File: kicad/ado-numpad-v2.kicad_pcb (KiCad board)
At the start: 2 copper layers, 99.5 x 96.8 mm, 39 parts, among them J1 Conn_01x04, J2 AudioJack4, SW1 SW_Push, SW10 SW_Push, SW11 SW_Push, SW12 SW_Push, SW13 SW_Push, SW14 SW_Push, SW15 SW_Push, SW16 SW_Push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

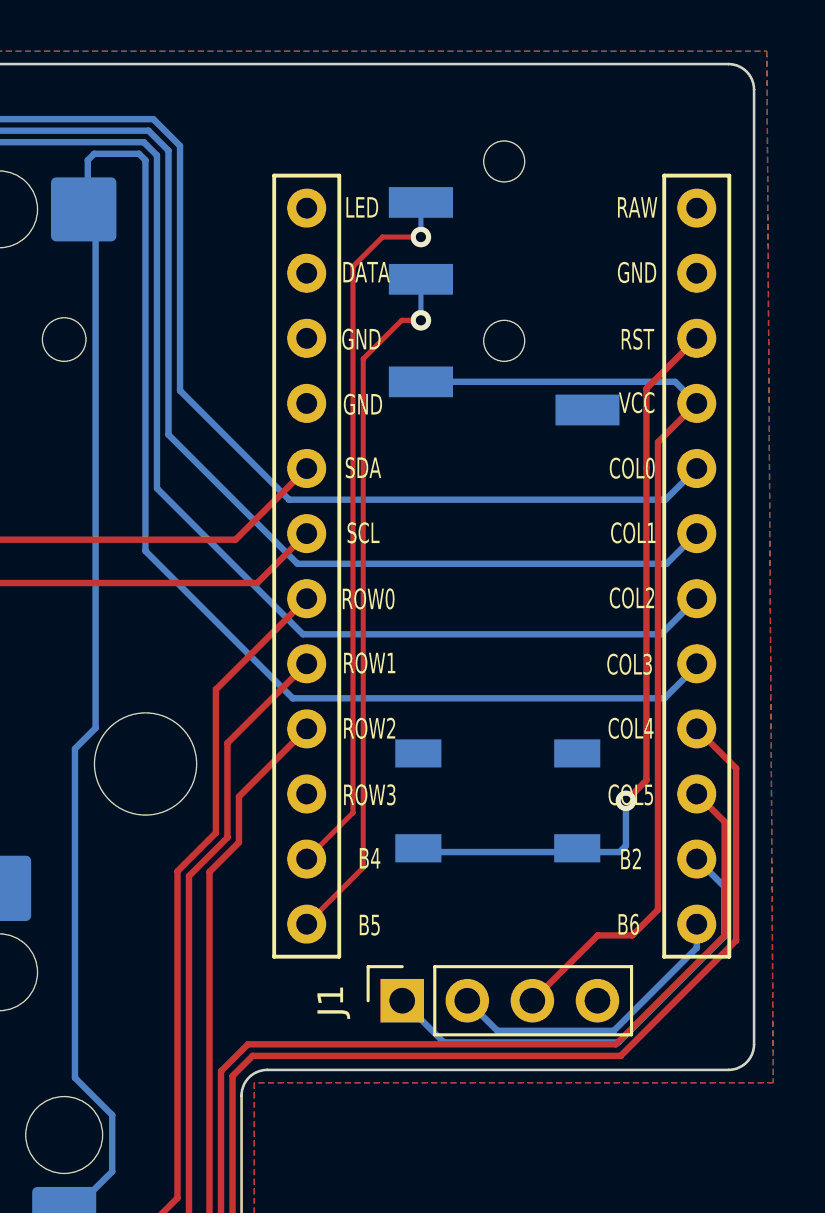
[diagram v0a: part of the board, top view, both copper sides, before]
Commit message: Update to use 2 1x12_P2.54mm Pin Sockets
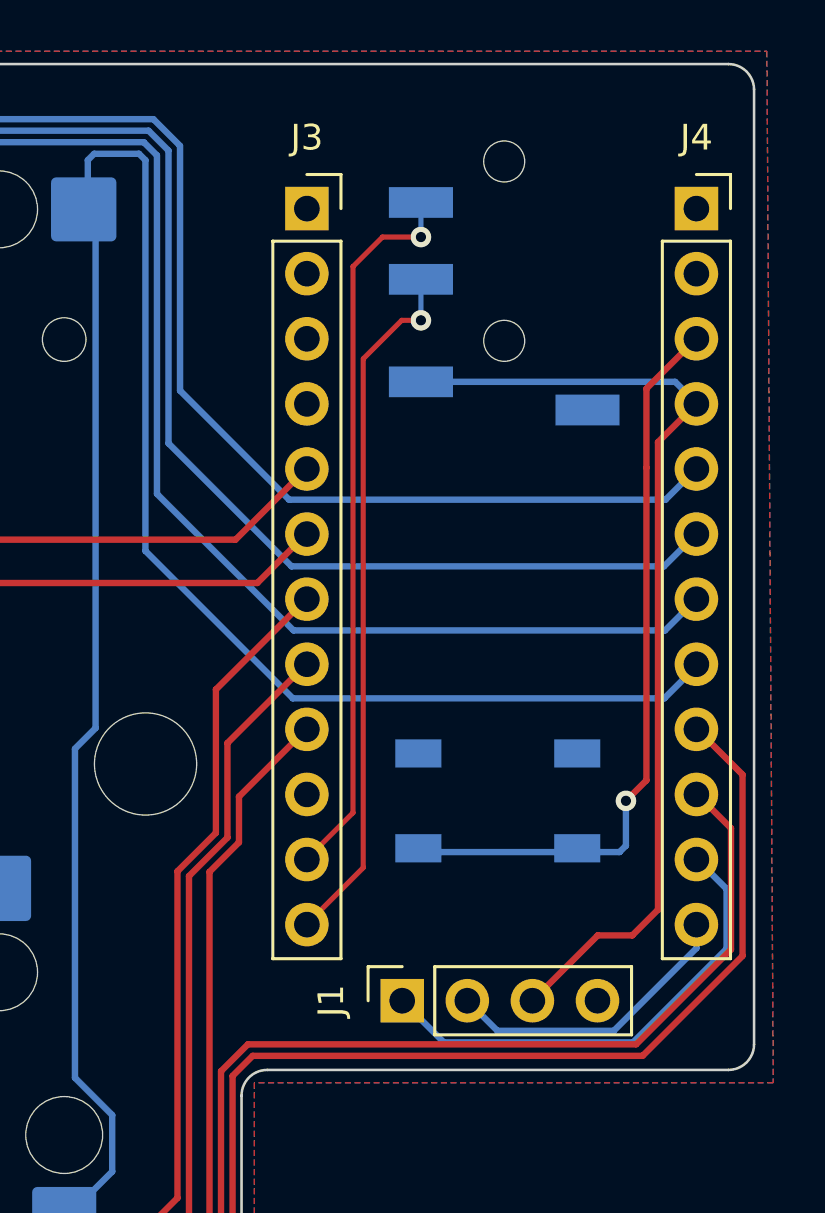
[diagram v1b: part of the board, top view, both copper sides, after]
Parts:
- removed U1: ProMicro, kbd:ProMicro_v2_1side
- added J3: Conn_01x12, Connector_PinSocket_2.54mm:PinSocket_1x12_P2.54mm_Vertical, F.Cu at (172.8, 57.1)
- added J4: Conn_01x12, Connector_PinSocket_2.54mm:PinSocket_1x12_P2.54mm_Vertical, F.Cu at (188.0, 57.1)
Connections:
- SW19 pad 2: RESET -> Net-(J4-Pin_3)
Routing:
- net RESET: track 29.0 -> 0.00 mm, vias 1 -> 0
- net Net-(J4-Pin_3): track 0.00 -> 29.0 mm, vias 0 -> 1
- net Enc_B: track 262.9 -> 263.6 mm
- net Enc_A: track 250.9 -> 251.6 mm

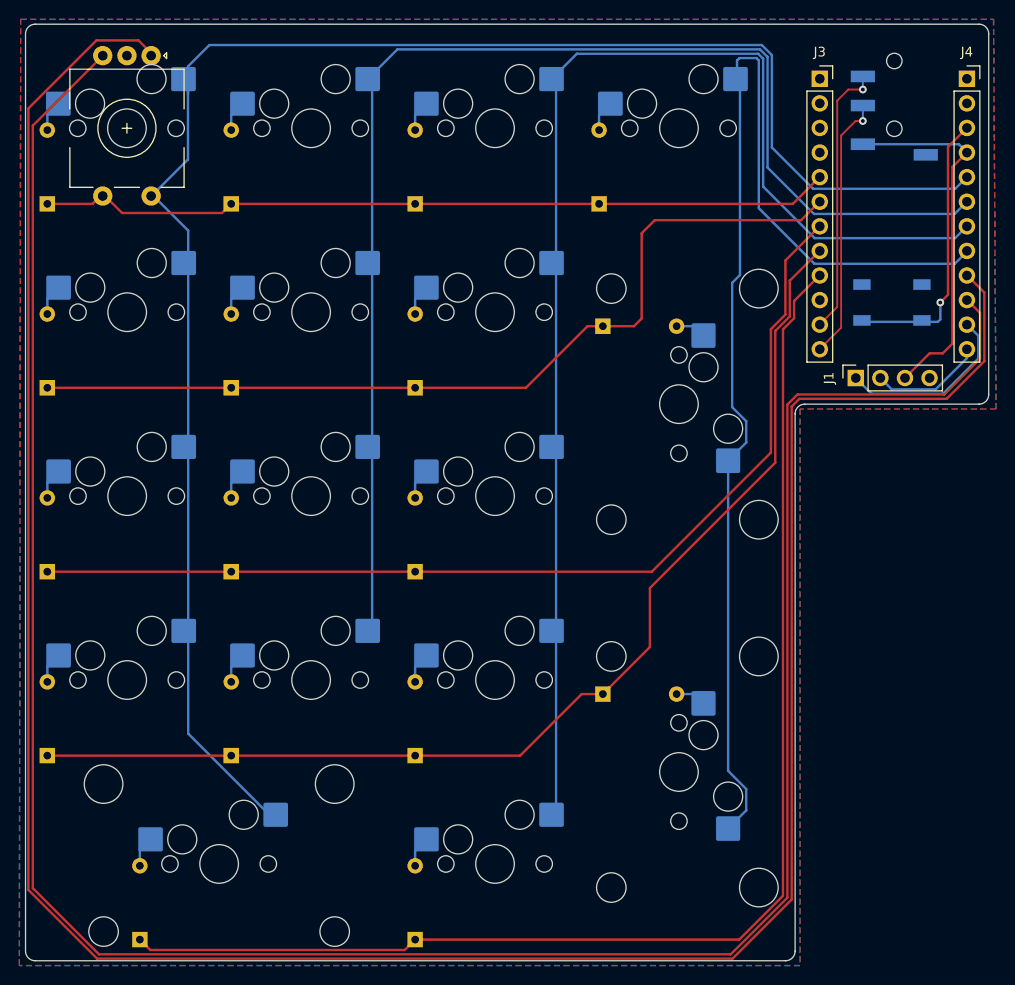
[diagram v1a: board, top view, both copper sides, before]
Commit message: Move Enc pins to Pin 1 and 2 on Pro Micro
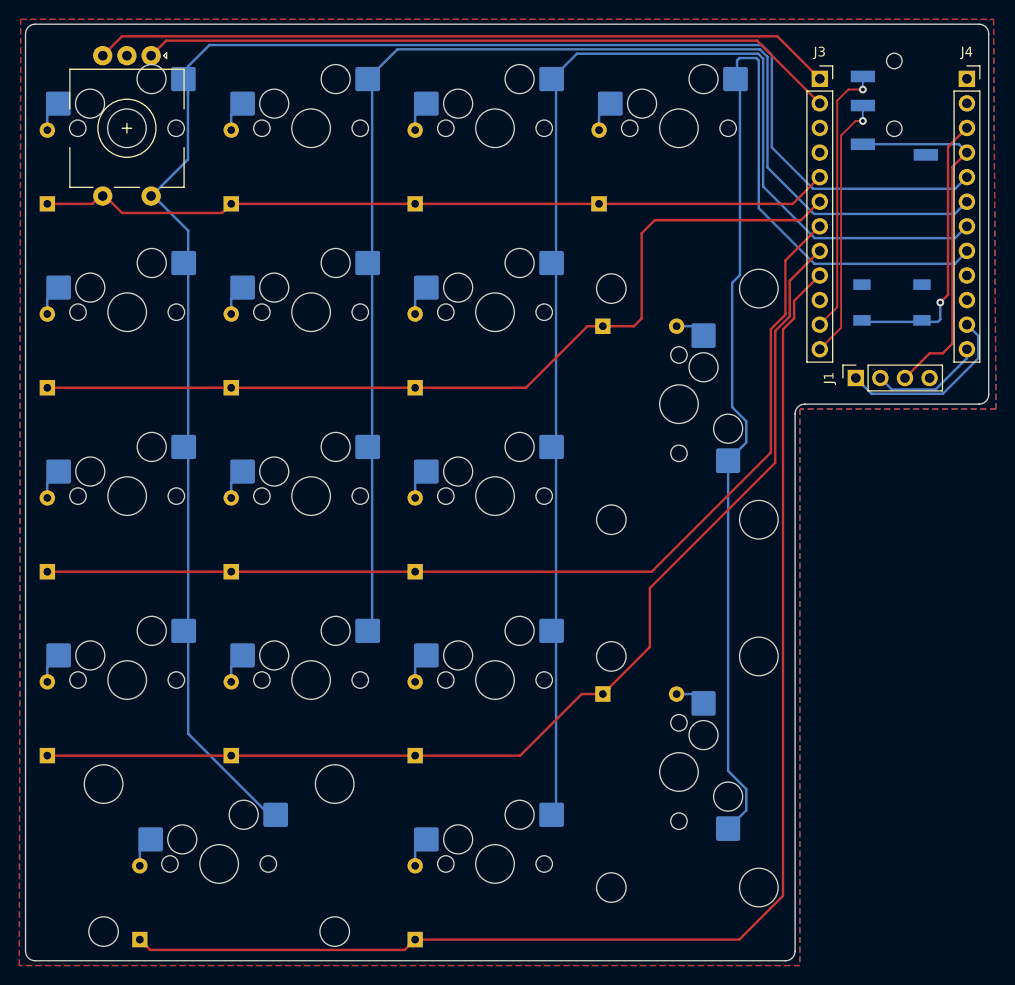
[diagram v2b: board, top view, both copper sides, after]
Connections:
- J3 pad 1: unconnected-(J3-Pin_1-Pad1) -> Enc_A
- J3 pad 2: unconnected-(J3-Pin_2-Pad2) -> Enc_B
- J4 pad 10: Enc_A -> unconnected-(J4-Pin_10-Pad10)
- J4 pad 9: Enc_B -> unconnected-(J4-Pin_9-Pad9)
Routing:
- net Enc_B: track 263.6 -> 72.4 mm
- net Enc_A: track 251.6 -> 76.7 mm
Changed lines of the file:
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@@
   (net 34 "SPLIT_COMMS+")
   (net 35 "Net-(J4-Pin_3)")
-  (net 36 "unconnected-(J3-Pin_1-Pad1)")
-  (net 37 "unconnected-(J3-Pin_2-Pad2)")
+  (net 36 "unconnected-(J4-Pin_9-Pad9)")
+  (net 37 "unconnected-(J4-Pin_10-Pad10)")
   (net 38 "unconnected-(J3-Pin_10-Pad10)")
   (net 39 "unconnected-(J4-Pin_1-Pad1)")
@@
       (stroke (width 0.1) (type solid)) (layer "F.Fab"))
     (pad "1" thru_hole rect (at 0 0) (size 1.7 1.7) (drill 1) (layers "*.Cu" "*.Mask")
-      (net 36 "unconnected-(J3-Pin_1-Pad1)") (pinfunction "Pin_1") (pintype "passive+no_connect"))
+      (net 6 "Enc_A") (pinfunction "Pin_1") (pintype "passive"))
     (pad "2" thru_hole oval (at 0 2.54) (size 1.7 1.7) (drill 1) (layers "*.Cu" "*.Mask")
-      (net 37 "unconnected-(J3-Pin_2-Pad2)") (pinfunction "Pin_2") (pintype "passive+no_connect"))
+      (net 7 "Enc_B") (pinfunction "Pin_2") (pintype "passive"))
     (pad "3" thru_hole oval (at 0 5.08) (size 1.7 1.7) (drill 1) (layers "*.Cu" "*.Mask")
       (net 5 "GND") (pinfunction "Pin_3") (pintype "passive"))
@@
       (net 8 "Col3") (pinfunction "Pin_8") (pintype "passive"))
     (pad "9" thru_hole oval (at 0 20.32) (size 1.7 1.7) (drill 1) (layers "*.Cu" "*.Mask")
-      (net 7 "Enc_B") (pinfunction "Pin_9") (pintype "passive"))
+      (net 36 "unconnected-(J4-Pin_9-Pad9)") (pinfunction "Pin_9") (pintype "passive+no_connect"))
     (pad "10" thru_hole oval (at 0 22.86) (size 1.7 1.7) (drill 1) (layers "*.Cu" "*.Mask")
-      (net 6 "Enc_A") (pinfunction "Pin_10") (pintype "passive"))
+      (net 37 "unconnected-(J4-Pin_10-Pad10)") (pinfunction "Pin_10") (pintype "passive+no_connect"))
     (pad "11" thru_hole oval (at 0 25.4) (size 1.7 1.7) (drill 1) (layers "*.Cu" "*.Mask")
       (net 32 "SCL") (pinfunction "Pin_11") (pintype "passive"))
@@
   (segment (start 170.15 80.0856) (end 170.15 81.872792) (width 0.25) (layer "F.Cu") (net 4))
   (segment (start 172.7936 77.442) (end 170.15 80.0856) (width 0.25) (layer "F.Cu") (net 4))
-  (segment (start 98.726192 54.761904) (end 98.726192 54.75) (width 0.25) (layer "F.Cu") (net 6))
-  (segment (start 170.5 89.75) (end 169.45 90.8) (width 0.25) (layer "F.Cu") (net 6))
-  (segment (start 163.595527 147.584) (end 98.334 147.584) (width 0.25) (layer "F.Cu") (net 6))
-  (segment (start 185.65 89.75) (end 170.5 89.75) (width 0.25) (layer "F.Cu") (net 6))
-  (segment (start 169.45 90.8) (end 169.45 141.729527) (width 0.25) (layer "F.Cu") (net 6))
-  (segment (start 91.5 61.988096) (end 98.726192 54.761904) (width 0.25) (layer "F.Cu") (net 6))
-  (segment (start 189.35 81.3184) (end 189.35 86.05) (width 0.25) (layer "F.Cu") (net 6))
-  (segment (start 189.35 86.05) (end 185.65 89.75) (width 0.25) (layer "F.Cu") (net 6))
-  (segment (start 188.0136 79.982) (end 189.35 81.3184) (width 0.25) (layer "F.Cu") (net 6))
-  (segment (start 169.45 141.729527) (end 163.595527 147.584) (width 0.25) (layer "F.Cu") (net 6))
-  (segment (start 98.334 147.584) (end 91.5 140.75) (width 0.25) (layer "F.Cu") (net 6))
-  (segment (start 91.5 140.75) (end 91.5 61.988096) (width 0.25) (layer "F.Cu") (net 6))
-  (segment (start 91.05 140.936396) (end 98.147604 148.034) (width 0.25) (layer "F.Cu") (net 7))
-  (segment (start 163.781923 148.034) (end 169.9 141.915923) (width 0.25) (layer "F.Cu") (net 7))
-  (segment (start 91.05 60.2) (end 91.05 140.936396) (width 0.25) (layer "F.Cu") (net 7))
-  (segment (start 102.425 53.175) (end 98.075 53.175) (width 0.25) (layer "F.Cu") (net 7))
-  (segment (start 103.75 54.5) (end 102.425 53.175) (width 0.25) (layer "F.Cu") (net 7))
-  (segment (start 185.9 90.2) (end 189.8 86.3) (width 0.25) (layer "F.Cu") (net 7))
-  (segment (start 189.8 79.2284) (end 188.0136 77.442) (width 0.25) (layer "F.Cu") (net 7))
-  (segment (start 169.9 141.915923) (end 169.9 90.986396) (width 0.25) (layer "F.Cu") (net 7))
-  (segment (start 169.9 90.986396) (end 170.686396 90.2) (width 0.25) (layer "F.Cu") (net 7))
-  (segment (start 170.686396 90.2) (end 185.9 90.2) (width 0.25) (layer "F.Cu") (net 7))
-  (segment (start 189.8 86.3) (end 189.8 79.2284) (width 0.25) (layer "F.Cu") (net 7))
-  (segment (start 98.147604 148.034) (end 163.781923 148.034) (width 0.25) (layer "F.Cu") (net 7))
-  (segment (start 98.075 53.175) (end 91.05 60.2) (width 0.25) (layer "F.Cu") (net 7))
+  (segment (start 98.726192 54.75) (end 100.726192 52.75) (width 0.25) (layer "F.Cu") (net 6))
+  (segment (start 100.726192 52.75) (end 168.41 52.75) (width 0.25) (layer "F.Cu") (net 6))
+  (segment (start 168.41 52.75) (end 172.8 57.14) (width 0.25) (layer "F.Cu") (net 6))
+  (segment (start 103.726192 54.75) (end 105.276192 53.2) (width 0.25) (layer "F.Cu") (net 7))
+  (segment (start 105.276192 53.2) (end 166.32 53.2) (width 0.25) (layer "F.Cu") (net 7))
+  (segment (start 166.32 53.2) (end 172.8 59.68) (width 0.25) (layer "F.Cu") (net 7))
   (segment (start 163.75 91.05835) (end 165.205 92.51335) (width 0.25) (layer "B.Cu") (net 8))
   (segment (start 186.75 76.25) (end 188.0136 74.9864) (width 0.25) (layer "B.Cu") (net 8))
